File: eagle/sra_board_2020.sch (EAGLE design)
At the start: 45 parts, among them Q2 IRF9530, SW1 DTS-6, SW2 DTS-6, SW3 DTS-6, SW4 DTS-6, U1 ESP32-DEVKITC-32D, X1 057-006-1

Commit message: Renamed Eagle files and Added Series Resistor Between ESP and Motor Driver
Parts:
- added R2, R3, R4, R5, R6, R7, R8, R9: 1KΩ, rcl:R-EU_0204/7
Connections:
- new net N$10: R9.1, TB2.BIN2
- new net N$3: R2.1, TB1.AIN2
- new net N$4: R3.1, TB1.AIN1
- new net N$5: R4.1, TB1.BIN1
- new net N$6: R5.1, TB1.BIN2
- new net N$7: R6.1, TB2.AIN2
- new net N$8: R7.1, TB2.AIN1
- new net N$9: R8.1, TB2.BIN1
- net 12: now also R8.2; no longer TB2.BIN1
- net 13: now also R9.2; no longer TB2.BIN2
- net 15: no longer TB1.STBY
- net 25: now also R4.2; no longer TB1.BIN1
- net 26: now also R5.2; no longer TB1.BIN2
- net AIN1: now also R3.2; no longer TB1.AIN1
- net AIN2: now also R2.2; no longer TB1.AIN2
- net BIN1: now also R7.2; no longer TB2.AIN1
- net BIN2: now also R6.2; no longer TB2.AIN2
- net O: no longer TB2.STBY
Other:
- moved on the sheet: AMS1117, CIN, CO, CO2, D1, FD, JP1, JP2, JP6, L1, LDZ1-1, LDZ1-10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

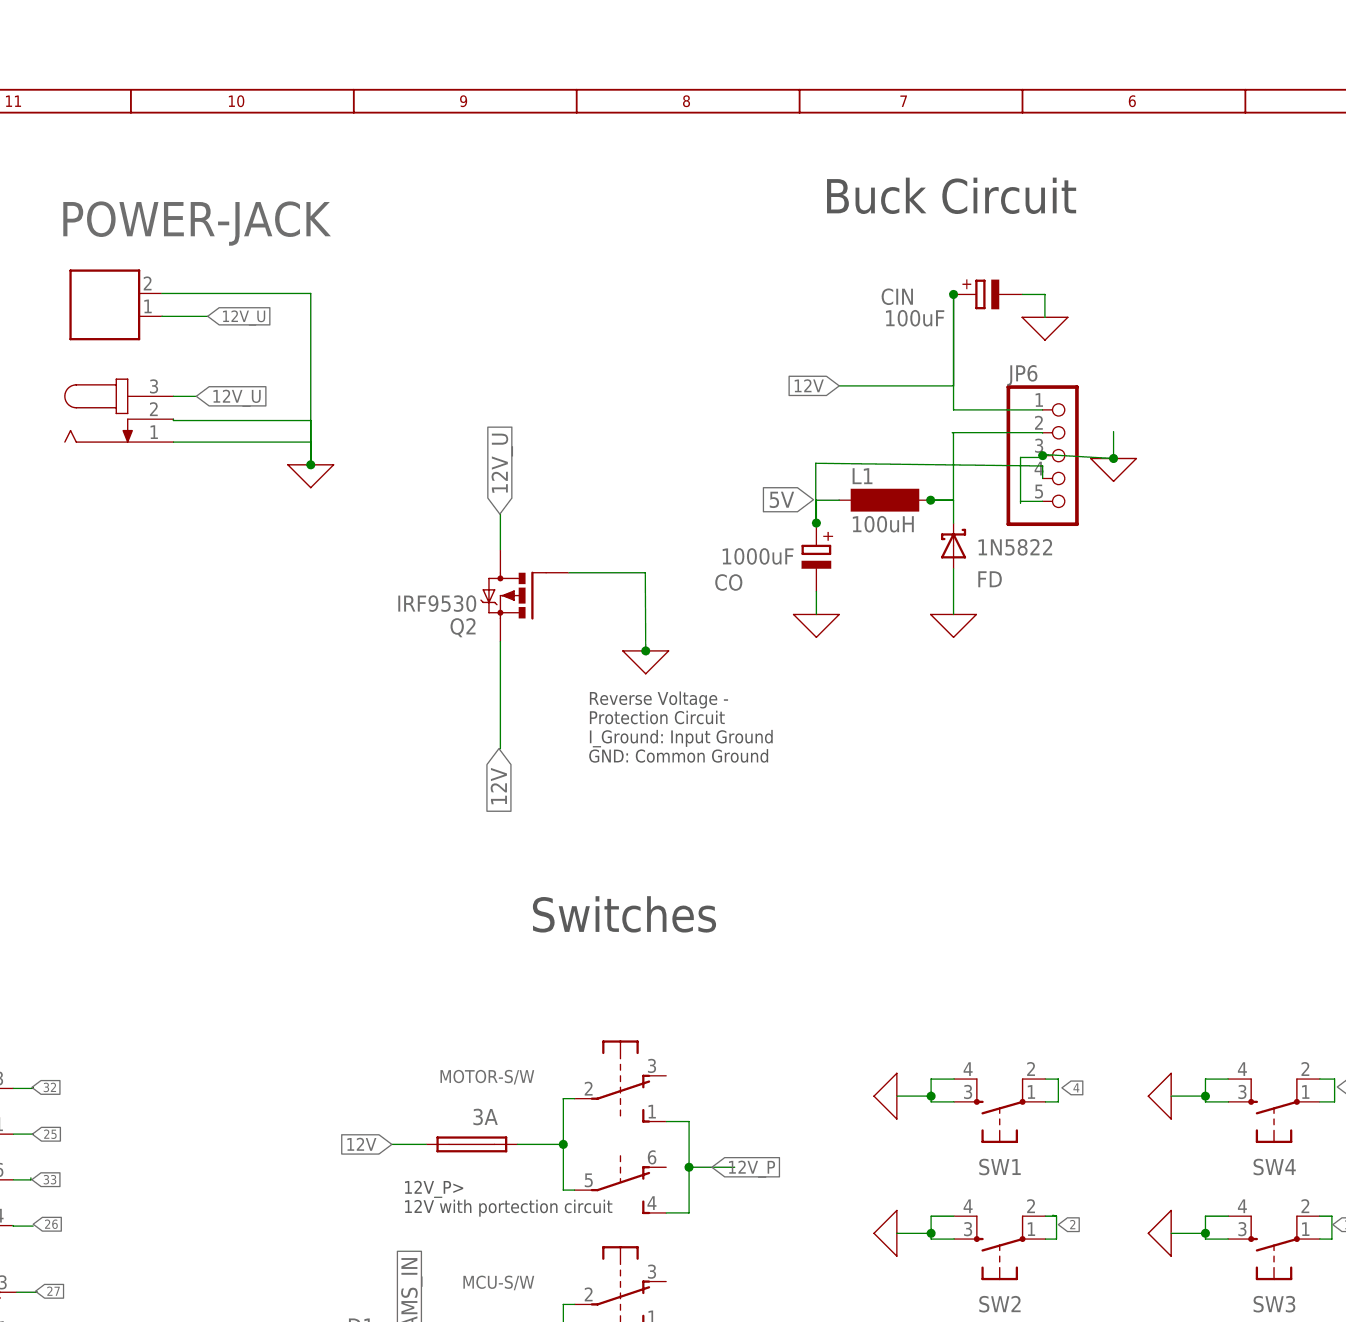
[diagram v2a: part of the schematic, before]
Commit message: Mosfet Replaced by two individual Diodes
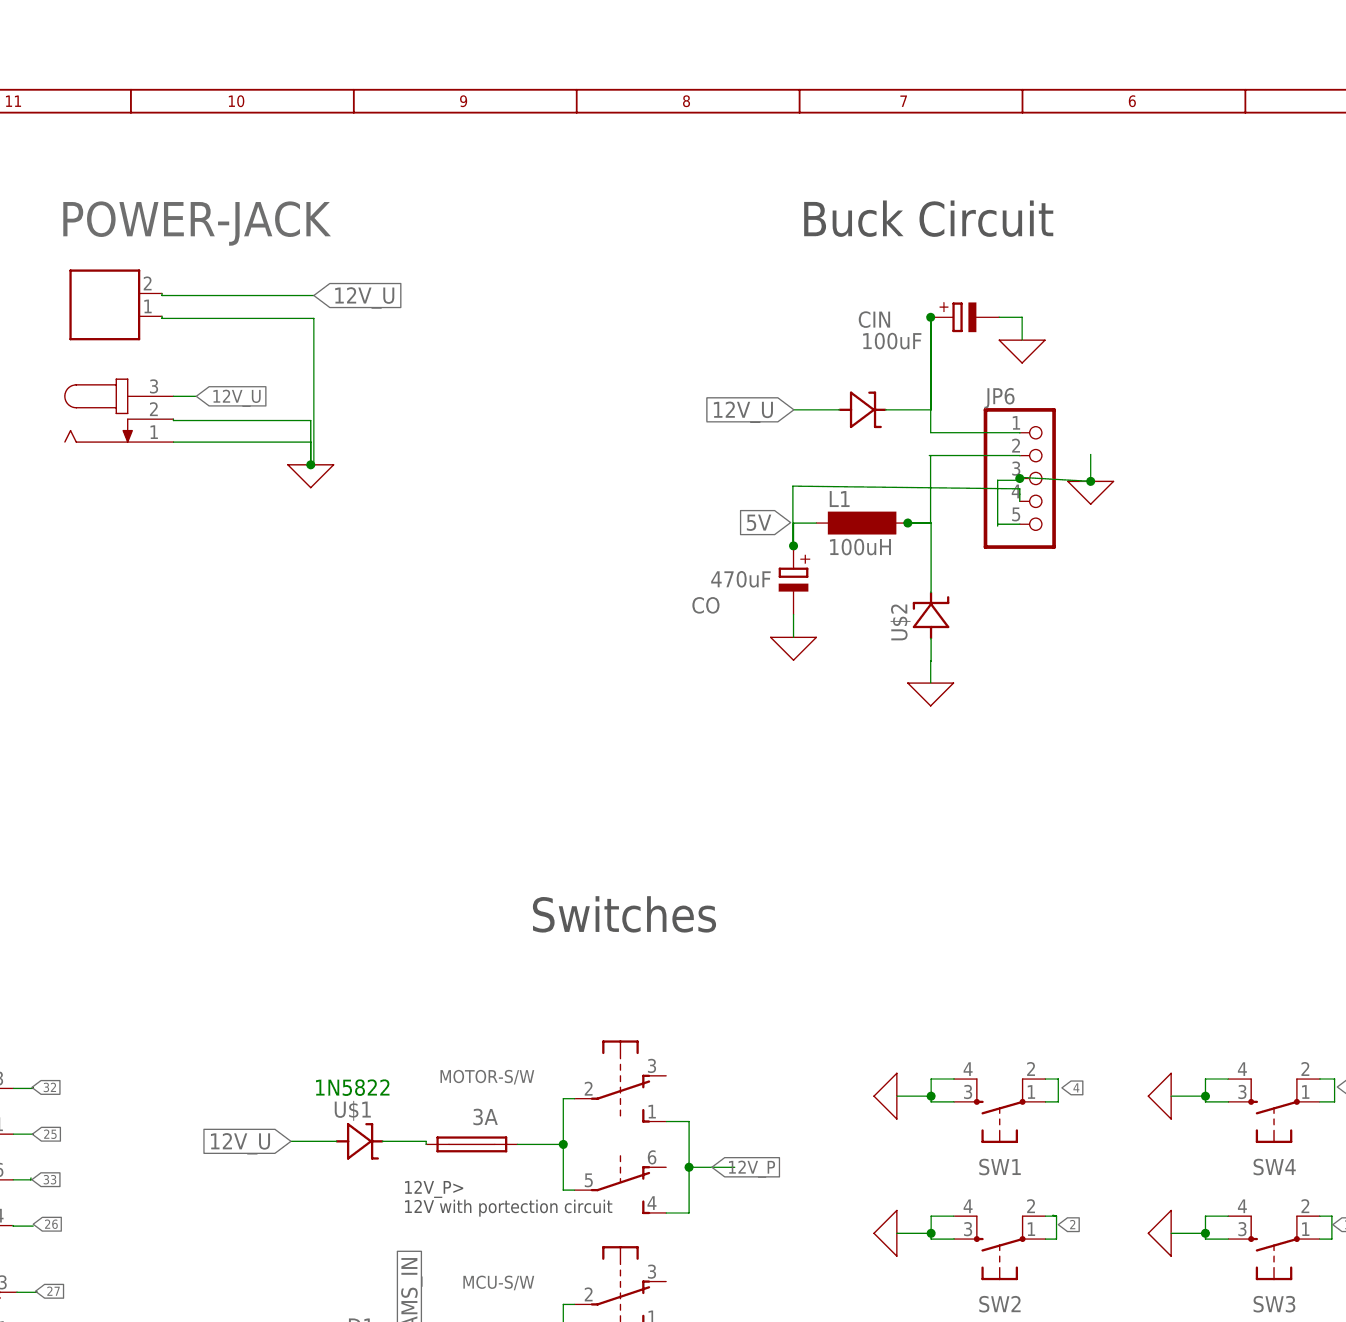
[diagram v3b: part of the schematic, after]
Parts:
- removed FD: 1N5822, 1N5822:1N5822
- removed Q2: IRF9530, transistor-power:IRF9530
- added U$1, U$2: 1N5399_SQUARE, diode_updated:1N5399_SQUARE
- added U$3: 1N5399_ROUND, diode_updated:1N5399_ROUND
- CO: value 1000uF -> 470uF
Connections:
- removed net 12V: CIN.+, F3.1, JP6.1, Q2.S
- new net N$12: F3.1, U$1.C
- new net N$13: CIN.+, JP6.1, U$3.C
- net 0: now also 12V.1, U$2.A; no longer 12V.2, FD.A, Q2.G
- net 12V_U: now also 12V.2, U$1.A, U$3.A; no longer 12V.1, Q2.D
- net N$11: now also U$2.C; no longer FD.C
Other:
- note added: "1N5822"
- note removed: "Reverse Voltage - Protection Circuit I_Ground: Input Ground GND: Common Ground"
- moved on the sheet: CIN, CO, JP6, L1

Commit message: Front and back silkscreen improved
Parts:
- added OLED: (no value), pinhead:PINHD-1X4
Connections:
- net 0: now also OLED.2
- net 21: now also OLED.3
- net 22: now also OLED.4
- net 3.3V: now also OLED.1, TB1.STBY, TB2.STBY
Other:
- note added: "22 - SDA 21 - SCL 23 - INT"
- note added: "Sensors ports"
- note removed: "Sensors"
- moved on the sheet: JP1, JP2, U1
